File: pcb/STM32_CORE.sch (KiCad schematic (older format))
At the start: 31 parts, among them J6 Conn_01x14, J7 Conn_01x12, J8 Conn_01x12, SW1 SW_Push, U3 STM32F103C8T6, U4 AMS1117-3.3, Y1 O8M, Y2 O32.768K

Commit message: update,
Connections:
- net PA2 renamed IONAIR-TTL-TX
- net PA3 renamed IONAIR-TTL-RX
- net PA6 renamed STM32_WS2812_OUTPUT
- net PB0 renamed STM32_SSR-25-DA_OUTPUT
- net PB1 renamed STM32_SSR_OUTPUT
- net PB3 renamed SPI1_SCK
- net PB4 renamed SPI1_MISO
- net PB5 renamed SPI1_MOSI
- net PB6 renamed STM32_FAN_PWM_OUTPUT
- net PB8 renamed I2C_SCL
- net PB9 renamed I2C_SDA
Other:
- moved on the sheet: C2, C3, C4, C5, C6
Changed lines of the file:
@@
 L taobao-c:C104 C3
 U 1 1 5BCBC4D6
-P 7850 5850
-F 0 "C3" H 7942 5896 50  0000 L CNN
-F 1 "C104" H 7942 5805 50  0000 L CNN
-F 2 "Capacitor_SMD:C_0603_1608Metric_Pad1.05x0.95mm_HandSolder" H 7850 5850 50  0001 C CNN
-F 3 "~" H 7850 5850 50  0001 C CNN
-	1    7850 5850
-	1    0    0    -1
-$EndComp
-Wire Wire Line
-	7850 5650 7850 5750
+P 7850 6800
+F 0 "C3" H 7942 6846 50  0000 L CNN
+F 1 "C104" H 7942 6755 50  0000 L CNN
+F 2 "Capacitor_SMD:C_0603_1608Metric_Pad1.05x0.95mm_HandSolder" H 7850 6800 50  0001 C CNN
+F 3 "~" H 7850 6800 50  0001 C CNN
+	1    7850 6800
+	1    0    0    -1
+$EndComp
+Wire Wire Line
+	7850 6600 7850 6700
 $Comp
 L power:GND #PWR026
 U 1 1 5BCBCE91
-P 7850 6050
-F 0 "#PWR026" H 7850 5800 50  0001 C CNN
-F 1 "GND" H 7855 5877 50  0000 C CNN
-F 2 "" H 7850 6050 50  0001 C CNN
-F 3 "" H 7850 6050 50  0001 C CNN
-	1    7850 6050
-	1    0    0    -1
-$EndComp
-Wire Wire Line
-	7850 5950 7850 6050
+P 7850 7000
+F 0 "#PWR026" H 7850 6750 50  0001 C CNN
+F 1 "GND" H 7855 6827 50  0000 C CNN
+F 2 "" H 7850 7000 50  0001 C CNN
+F 3 "" H 7850 7000 50  0001 C CNN
+	1    7850 7000
+	1    0    0    -1
+$EndComp
+Wire Wire Line
+	7850 6900 7850 7000
 $Comp
 L taobao-c:C104 C4
 U 1 1 5BCBD860
-P 8300 5850
-F 0 "C4" H 8392 5896 50  0000 L CNN
-F 1 "C104" H 8392 5805 50  0000 L CNN
-F 2 "Capacitor_SMD:C_0603_1608Metric_Pad1.05x0.95mm_HandSolder" H 8300 5850 50  0001 C CNN
-F 3 "~" H 8300 5850 50  0001 C CNN
-	1    8300 5850
-	1    0    0    -1
-$EndComp
-Wire Wire Line
-	8300 5650 8300 5750
+P 8300 6800
+F 0 "C4" H 8392 6846 50  0000 L CNN
+F 1 "C104" H 8392 6755 50  0000 L CNN
+F 2 "Capacitor_SMD:C_0603_1608Metric_Pad1.05x0.95mm_HandSolder" H 8300 6800 50  0001 C CNN
+F 3 "~" H 8300 6800 50  0001 C CNN
+	1    8300 6800
+	1    0    0    -1
+$EndComp
+Wire Wire Line
+	8300 6600 8300 6700
 $Comp
 L power:GND #PWR028
 U 1 1 5BCBD867
-P 8300 6050
-F 0 "#PWR028" H 8300 5800 50  0001 C CNN
-F 1 "GND" H 8305 5877 50  0000 C CNN
-F 2 "" H 8300 6050 50  0001 C CNN
-F 3 "" H 8300 6050 50  0001 C CNN
-	1    8300 6050
-	1    0    0    -1
-$EndComp
-Wire Wire Line
-	8300 5950 8300 6050
+P 8300 7000
+F 0 "#PWR028" H 8300 6750 50  0001 C CNN
+F 1 "GND" H 8305 6827 50  0000 C CNN
+F 2 "" H 8300 7000 50  0001 C CNN
+F 3 "" H 8300 7000 50  0001 C CNN
+	1    8300 7000
+	1    0    0    -1
+$EndComp
+Wire Wire Line
+	8300 6900 8300 7000
 $Comp
 L taobao-c:C104 C5
 U 1 1 5BCBE2F2
-P 8700 5850
-F 0 "C5" H 8792 5896 50  0000 L CNN
-F 1 "C104" H 8792 5805 50  0000 L CNN
-F 2 "Capacitor_SMD:C_0603_1608Metric_Pad1.05x0.95mm_HandSolder" H 8700 5850 50  0001 C CNN
-F 3 "~" H 8700 5850 50  0001 C CNN
-	1    8700 5850
-	1    0    0    -1
-$EndComp
-Wire Wire Line
-	8700 5650 8700 5750
+P 8700 6800
+F 0 "C5" H 8792 6846 50  0000 L CNN
+F 1 "C104" H 8792 6755 50  0000 L CNN
+F 2 "Capacitor_SMD:C_0603_1608Metric_Pad1.05x0.95mm_HandSolder" H 8700 6800 50  0001 C CNN
+F 3 "~" H 8700 6800 50  0001 C CNN
+	1    8700 6800
+	1    0    0    -1
+$EndComp
+Wire Wire Line
+	8700 6600 8700 6700
 $Comp
 L power:GND #PWR030
 U 1 1 5BCBE2F9
-P 8700 6050
-F 0 "#PWR030" H 8700 5800 50  0001 C CNN
-F 1 "GND" H 8705 5877 50  0000 C CNN
-F 2 "" H 8700 6050 50  0001 C CNN
-F 3 "" H 8700 6050 50  0001 C CNN
-	1    8700 6050
-	1    0    0    -1
-$EndComp
-Wire Wire Line
-	8700 5950 8700 6050
+P 8700 7000
+F 0 "#PWR030" H 8700 6750 50  0001 C CNN
+F 1 "GND" H 8705 6827 50  0000 C CNN
+F 2 "" H 8700 7000 50  0001 C CNN
+F 3 "" H 8700 7000 50  0001 C CNN
+	1    8700 7000
+	1    0    0    -1
+$EndComp
+Wire Wire Line
+	8700 6900 8700 7000
 $Comp
 L taobao-c:C104 C6
 U 1 1 5BCBE306
-P 9150 5850
-F 0 "C6" H 9242 5896 50  0000 L CNN
-F 1 "C104" H 9242 5805 50  0000 L CNN
-F 2 "Capacitor_SMD:C_0603_1608Metric_Pad1.05x0.95mm_HandSolder" H 9150 5850 50  0001 C CNN
-F 3 "~" H 9150 5850 50  0001 C CNN
-	1    9150 5850
-	1    0    0    -1
-$EndComp
-Wire Wire Line
-	9150 5650 9150 5750
+P 9150 6800
+F 0 "C6" H 9242 6846 50  0000 L CNN
+F 1 "C104" H 9242 6755 50  0000 L CNN
+F 2 "Capacitor_SMD:C_0603_1608Metric_Pad1.05x0.95mm_HandSolder" H 9150 6800 50  0001 C CNN
+F 3 "~" H 9150 6800 50  0001 C CNN
+	1    9150 6800
+	1    0    0    -1
+$EndComp
+Wire Wire Line
+	9150 6600 9150 6700
 $Comp
 L power:GND #PWR032
 U 1 1 5BCBE30D
-P 9150 6050
-F 0 "#PWR032" H 9150 5800 50  0001 C CNN
-F 1 "GND" H 9155 5877 50  0000 C CNN
-F 2 "" H 9150 6050 50  0001 C CNN
-F 3 "" H 9150 6050 50  0001 C CNN
-	1    9150 6050
-	1    0    0    -1
-$EndComp
-Wire Wire Line
-	9150 5950 9150 6050
+P 9150 7000
+F 0 "#PWR032" H 9150 6750 50  0001 C CNN
+F 1 "GND" H 9155 6827 50  0000 C CNN
+F 2 "" H 9150 7000 50  0001 C CNN
+F 3 "" H 9150 7000 50  0001 C CNN
+	1    9150 7000
+	1    0    0    -1
+$EndComp
+Wire Wire Line
+	9150 6900 9150 7000
 $Comp
 L taobao-osc:O32.768K Y2
@@
 L taobao-c:C104 C2
 U 1 1 5BD956B7
-P 5950 2200
-F 0 "C2" H 6042 2246 50  0000 L CNN
-F 1 "C104" H 6042 2155 50  0000 L CNN
-F 2 "Capacitor_SMD:C_0603_1608Metric_Pad1.05x0.95mm_HandSolder" H 5950 2200 50  0001 C CNN
-F 3 "~" H 5950 2200 50  0001 C CNN
-F 4 "near SWD" H 5950 2200 50  0001 C CNN "Field4"
-	1    5950 2200
+P 5250 1550
+F 0 "C2" H 5342 1596 50  0000 L CNN
+F 1 "C104" H 5342 1505 50  0000 L CNN
+F 2 "Capacitor_SMD:C_0603_1608Metric_Pad1.05x0.95mm_HandSolder" H 5250 1550 50  0001 C CNN
+F 3 "~" H 5250 1550 50  0001 C CNN
+F 4 "near SWD" H 5250 1550 50  0001 C CNN "Field4"
+	1    5250 1550
 	1    0    0    -1
 $EndComp
@@
 L power:GND #PWR023
 U 1 1 5BD957D4
-P 5950 2450
-F 0 "#PWR023" H 5950 2200 50  0001 C CNN
-F 1 "GND" H 5955 2277 50  0000 C CNN
-F 2 "" H 5950 2450 50  0001 C CNN
-F 3 "" H 5950 2450 50  0001 C CNN
-	1    5950 2450
-	1    0    0    -1
-$EndComp
-Wire Wire Line
-	5950 2300 5950 2450
-Wire Wire Line
-	5950 1950 5950 2100
+P 5250 1800
+F 0 "#PWR023" H 5250 1550 50  0001 C CNN
+F 1 "GND" H 5255 1627 50  0000 C CNN
+F 2 "" H 5250 1800 50  0001 C CNN
+F 3 "" H 5250 1800 50  0001 C CNN
+	1    5250 1800
+	1    0    0    -1
+$EndComp
+Wire Wire Line
+	5250 1650 5250 1800
+Wire Wire Line
+	5250 1300 5250 1450
 Text Label 2350 2600 2    50   ~ 0
 SWIO
@@
 	1    0    0    1
 $EndComp
-Text Label 6300 2350 1    50   ~ 0
+Text Label 5600 1700 1    50   ~ 0
 VCC3V3
 Wire Wire Line
-	6300 1950 6300 2350
+	5600 1300 5600 1700
 $Comp
 L Device:Jumper_NO_Small JP1
@@
 L power:+3V3 #PWR024
 U 1 1 5BCAD5BF
-P 6300 1950
-F 0 "#PWR024" H 6300 1800 50  0001 C CNN
-F 1 "+3V3" H 6350 2150 50  0000 C CNN
-F 2 "" H 6300 1950 50  0001 C CNN
-F 3 "" H 6300 1950 50  0001 C CNN
-	1    6300 1950
+P 5600 1300
+F 0 "#PWR024" H 5600 1150 50  0001 C CNN
+F 1 "+3V3" H 5650 1500 50  0000 C CNN
+F 2 "" H 5600 1300 50  0001 C CNN
+F 3 "" H 5600 1300 50  0001 C CNN
+	1    5600 1300
 	1    0    0    -1
 $EndComp
@@
 L power:+3V3 #PWR025
 U 1 1 5BCBE3DE
-P 7850 5650
-F 0 "#PWR025" H 7850 5500 50  0001 C CNN
-F 1 "+3V3" H 7900 5850 50  0000 C CNN
-F 2 "" H 7850 5650 50  0001 C CNN
-F 3 "" H 7850 5650 50  0001 C CNN
-	1    7850 5650
+P 7850 6600
+F 0 "#PWR025" H 7850 6450 50  0001 C CNN
+F 1 "+3V3" H 7900 6800 50  0000 C CNN
+F 2 "" H 7850 6600 50  0001 C CNN
+F 3 "" H 7850 6600 50  0001 C CNN
+	1    7850 6600
 	1    0    0    -1
 $EndComp
@@
 L power:+3V3 #PWR027
 U 1 1 5BCE7C1D
-P 8300 5650
-F 0 "#PWR027" H 8300 5500 50  0001 C CNN
-F 1 "+3V3" H 8350 5850 50  0000 C CNN
-F 2 "" H 8300 5650 50  0001 C CNN
-F 3 "" H 8300 5650 50  0001 C CNN
-	1    8300 5650
+P 8300 6600
+F 0 "#PWR027" H 8300 6450 50  0001 C CNN
+F 1 "+3V3" H 8350 6800 50  0000 C CNN
+F 2 "" H 8300 6600 50  0001 C CNN
+F 3 "" H 8300 6600 50  0001 C CNN
+	1    8300 6600
 	1    0    0    -1
 $EndComp
@@
 L power:+3V3 #PWR029
 U 1 1 5BCE7C66
-P 8700 5650
-F 0 "#PWR029" H 8700 5500 50  0001 C CNN
-F 1 "+3V3" H 8750 5850 50  0000 C CNN
-F 2 "" H 8700 5650 50  0001 C CNN
-F 3 "" H 8700 5650 50  0001 C CNN
-	1    8700 5650
+P 8700 6600
+F 0 "#PWR029" H 8700 6450 50  0001 C CNN
+F 1 "+3V3" H 8750 6800 50  0000 C CNN
+F 2 "" H 8700 6600 50  0001 C CNN
+F 3 "" H 8700 6600 50  0001 C CNN
+	1    8700 6600
 	1    0    0    -1
 $EndComp
@@
 L power:+3V3 #PWR031
 U 1 1 5BCE7CAF
-P 9150 5650
-F 0 "#PWR031" H 9150 5500 50  0001 C CNN
-F 1 "+3V3" H 9200 5850 50  0000 C CNN
-F 2 "" H 9150 5650 50  0001 C CNN
-F 3 "" H 9150 5650 50  0001 C CNN
-	1    9150 5650
+P 9150 6600
+F 0 "#PWR031" H 9150 6450 50  0001 C CNN
+F 1 "+3V3" H 9200 6800 50  0000 C CNN
+F 2 "" H 9150 6600 50  0001 C CNN
+F 3 "" H 9150 6600 50  0001 C CNN
+	1    9150 6600
 	1    0    0    -1
 $EndComp
@@
 L power:+3V3 #PWR022
 U 1 1 5BCF284B
-P 5950 1950
-F 0 "#PWR022" H 5950 1800 50  0001 C CNN
-F 1 "+3V3" H 6000 2150 50  0000 C CNN
-F 2 "" H 5950 1950 50  0001 C CNN
-F 3 "" H 5950 1950 50  0001 C CNN
-	1    5950 1950
+P 5250 1300
+F 0 "#PWR022" H 5250 1150 50  0001 C CNN
+F 1 "+3V3" H 5300 1500 50  0000 C CNN
+F 2 "" H 5250 1300 50  0001 C CNN
+F 3 "" H 5250 1300 50  0001 C CNN
+	1    5250 1300
 	1    0    0    -1
 $EndComp
@@
 	0    -1   -1   0
 $EndComp
+Text GLabel 8100 1650 1    50   Input ~ 0
+I2C_SDA
+Text GLabel 8200 1650 1    50   Input ~ 0
+I2C_SCL
+Text GLabel 8600 1650 1    50   Input ~ 0
+SPI1_MOSI
+Text GLabel 8700 1650 1    50   Input ~ 0
+SPI1_MISO
+Text GLabel 8800 1650 1    50   Input ~ 0
+SPI1_SCK
+Text GLabel 8500 1650 1    50   Input ~ 0
+STM32_FAN_PWM_OUTPUT
+Text GLabel 8500 4750 3    50   Input ~ 0
+STM32_SSR_OUTPUT
+Text GLabel 8400 4750 3    50   Input ~ 0
+STM32_SSR-25-DA_OUTPUT
+Text GLabel 6900 3750 0    50   Input ~ 0
+IONAIR-TTL-TX
+Text GLabel 7900 4750 3    50   Input ~ 0
+IONAIR-TTL-RX
+Text GLabel 8200 4750 3    50   Input ~ 0
+STM32_WS2812_OUTPUT
 $EndSCHEMATC

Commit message: update,
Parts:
- J8: value Conn_01x12 -> Conn_01x15; footprint Connector_PinHeader_1.27mm:PinHeader_1x20_P1.27mm_Vertical -> Connector_PinHeader_1.27mm:PinHeader_1x15_P1.27mm_Vertical; symbol Connector_Generic:Conn_01x20 -> Connector_Generic:Conn_01x15
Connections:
- net PB13 is gone; now on net STM32_FAN_PWM_OUTPUT: J7.2 (Pin_2), U3.26 (PB13)
- net +3V3: now also J8.2 (Pin_2); no longer J8.3 (Pin_3)
- net GND: now also J8.1 (Pin_1); no longer J8.2 (Pin_2)
- net IONAIR-TTL-RX: now also J8.7 (Pin_7); no longer J8.12 (Pin_12)
- net IONAIR-TTL-TX: now also J8.6 (Pin_6); no longer J8.11 (Pin_11)
- net PA0: now also J8.4 (Pin_4); no longer J8.9 (Pin_9)
- net PA1: now also J8.5 (Pin_5); no longer J8.10 (Pin_10)
- net PA4: now also J8.8 (Pin_8); no longer J8.13 (Pin_13)
- net PA5: now also J8.9 (Pin_9); no longer J8.14 (Pin_14)
- net PA7: now also J8.11 (Pin_11); no longer J8.16 (Pin_16)
- net PB10: now also J8.14 (Pin_14); no longer J8.19 (Pin_19)
- net PB11: now also J8.15 (Pin_15); no longer J8.20 (Pin_20)
- net STM32_FAN_PWM_OUTPUT: no longer J6.9 (Pin_9), U3.42 (PB6)
- net STM32_SSR-25-DA_OUTPUT: now also J8.13 (Pin_13), U3.19 (PB1); no longer J8.17 (Pin_17), U3.18 (PB0)
- net STM32_SSR_OUTPUT: now also J8.12 (Pin_12), U3.18 (PB0); no longer J8.18 (Pin_18), U3.19 (PB1)
- net STM32_WS2812_OUTPUT: now also J8.10 (Pin_10); no longer J8.15 (Pin_15)
- new net PB6: J6.9 (Pin_9), U3.42 (PB6)
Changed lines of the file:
@@
 L power:GND #PWR019
 U 1 1 5BD5A437
-P 3850 4750
-F 0 "#PWR019" H 3850 4500 50  0001 C CNN
-F 1 "GND" H 3855 4577 50  0000 C CNN
-F 2 "" H 3850 4750 50  0001 C CNN
-F 3 "" H 3850 4750 50  0001 C CNN
-	1    3850 4750
+P 3850 4350
+F 0 "#PWR019" H 3850 4100 50  0001 C CNN
+F 1 "GND" H 3855 4177 50  0000 C CNN
+F 2 "" H 3850 4350 50  0001 C CNN
+F 3 "" H 3850 4350 50  0001 C CNN
+	1    3850 4350
 	1    0    0    -1
 $EndComp
@@
 $EndComp
 $Comp
-L Connector_Generic:Conn_01x20 J8
+L Connector_Generic:Conn_01x15 J8
 U 1 1 5BDCE49F
-P 4950 3900
-F 0 "J8" H 4869 2675 50  0000 C CNN
-F 1 "Conn_01x12" H 4869 2766 50  0000 C CNN
-F 2 "Connector_PinHeader_1.27mm:PinHeader_1x20_P1.27mm_Vertical" H 4950 3900 50  0001 C CNN
-F 3 "~" H 4950 3900 50  0001 C CNN
-	1    4950 3900
+P 4950 3600
+F 0 "J8" H 4869 2375 50  0000 C CNN
+F 1 "Conn_01x15" H 4869 2466 50  0000 C CNN
+F 2 "Connector_PinHeader_1.27mm:PinHeader_1x15_P1.27mm_Vertical" H 4950 3600 50  0001 C CNN
+F 3 "~" H 4950 3600 50  0001 C CNN
+	1    4950 3600
 	1    0    0    1
 $EndComp
@@
 	4350 3800 4750 3800
 Wire Wire Line
-	3850 4750 3850 4700
-Wire Wire Line
-	3850 4700 4750 4700
-Wire Wire Line
-	3950 4550 3950 4600
-Wire Wire Line
-	3950 4600 4750 4600
+	3850 4350 3850 4300
+Wire Wire Line
+	3850 4300 4750 4300
+Wire Wire Line
+	3950 4150 3950 4200
+Wire Wire Line
+	3950 4200 4750 4200
 Text Label 2000 3700 2    50   ~ 0
 PC13
@@
 L power:+3V3 #PWR020
 U 1 1 5BCACA2F
-P 3950 4550
-F 0 "#PWR020" H 3950 4400 50  0001 C CNN
-F 1 "+3V3" H 4000 4750 50  0000 C CNN
-F 2 "" H 3950 4550 50  0001 C CNN
-F 3 "" H 3950 4550 50  0001 C CNN
-	1    3950 4550
+P 3950 4150
+F 0 "#PWR020" H 3950 4000 50  0001 C CNN
+F 1 "+3V3" H 4000 4350 50  0000 C CNN
+F 2 "" H 3950 4150 50  0001 C CNN
+F 3 "" H 3950 4150 50  0001 C CNN
+	1    3950 4150
 	1    0    0    -1
 $EndComp
@@
 Text GLabel 8800 1650 1    50   Input ~ 0
 SPI1_SCK
-Text GLabel 8500 1650 1    50   Input ~ 0
+Text GLabel 10000 3650 2    50   Input ~ 0
 STM32_FAN_PWM_OUTPUT
+Text GLabel 8400 4750 3    50   Input ~ 0
+STM32_SSR_OUTPUT
 Text GLabel 8500 4750 3    50   Input ~ 0
-STM32_SSR_OUTPUT
-Text GLabel 8400 4750 3    50   Input ~ 0
 STM32_SSR-25-DA_OUTPUT
 Text GLabel 6900 3750 0    50   Input ~ 0

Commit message: update,
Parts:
- added J11: Conn_01x04, footprint-lib:Pin_Header_Straight_1x04_Pitch2.54mm, symbol Connector_Generic:Conn_01x04
- added J12: Conn_01x04, footprint-lib:Pin_Header_Straight_1x03_Pitch2.54mm, symbol Connector_Generic:Conn_01x03
- J6: footprint Connector_PinHeader_1.27mm:PinHeader_1x14_P1.27mm_Vertical -> footprint-lib:Pin_Header_Straight_1x14_Pitch1.27mm
- J7: footprint Connector_PinHeader_1.27mm:PinHeader_1x12_P1.27mm_Vertical -> footprint-lib:Pin_Header_Straight_1x12_Pitch1.27mm
- J8: footprint Connector_PinHeader_1.27mm:PinHeader_1x15_P1.27mm_Vertical -> footprint-lib:Pin_Header_Straight_1x15_Pitch1.27mm
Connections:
- net +3V3: now also J11.4 (Pin_4), J12.2 (Pin_2); no longer D2.2 (A), J6.1 (Pin_1)
- net +5V: now also D2.2 (A), J12.3 (Pin_3)
- net GND: now also J11.1 (Pin_1), J12.1 (Pin_1)
- net SWCLK: now also J11.2 (Pin_2)
- net SWIO: now also J11.3 (Pin_3)
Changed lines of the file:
@@
 Wire Wire Line
 	2250 3800 2250 3950
-Wire Wire Line
-	2150 2400 2150 2500
 $Comp
 L power:GND #PWR018
@@
 F 0 "J7" V 3467 1596 50  0000 C CNN
 F 1 "Conn_01x12" V 3376 1596 50  0000 C CNN
-F 2 "Connector_PinHeader_1.27mm:PinHeader_1x12_P1.27mm_Vertical" H 3250 1650 50  0001 C CNN
+F 2 "footprint-lib:Pin_Header_Straight_1x12_Pitch1.27mm" H 3250 1650 50  0001 C CNN
 F 3 "~" H 3250 1650 50  0001 C CNN
 	1    3250 1650
@@
 F 0 "J6" H 1420 3817 50  0000 C CNN
 F 1 "Conn_01x14" H 1420 3726 50  0000 C CNN
-F 2 "Connector_PinHeader_1.27mm:PinHeader_1x14_P1.27mm_Vertical" H 1500 3100 50  0001 C CNN
+F 2 "footprint-lib:Pin_Header_Straight_1x14_Pitch1.27mm" H 1500 3100 50  0001 C CNN
 F 3 "~" H 1500 3100 50  0001 C CNN
 	1    1500 3100
@@
 F 0 "J8" H 4869 2375 50  0000 C CNN
 F 1 "Conn_01x15" H 4869 2466 50  0000 C CNN
-F 2 "Connector_PinHeader_1.27mm:PinHeader_1x15_P1.27mm_Vertical" H 4950 3600 50  0001 C CNN
+F 2 "footprint-lib:Pin_Header_Straight_1x15_Pitch1.27mm" H 4950 3600 50  0001 C CNN
 F 3 "~" H 4950 3600 50  0001 C CNN
 	1    4950 3600
@@
 Wire Wire Line
 	1700 2600 2350 2600
-Wire Wire Line
-	1700 2500 2150 2500
 Text Label 4350 4000 0    50   ~ 0
 PA0
@@
 Wire Wire Line
 	2000 3700 1700 3700
-$Comp
-L power:+3V3 #PWR017
-U 1 1 5BCAC201
-P 2150 2400
-F 0 "#PWR017" H 2150 2250 50  0001 C CNN
-F 1 "+3V3" H 2200 2600 50  0000 C CNN
-F 2 "" H 2150 2400 50  0001 C CNN
-F 3 "" H 2150 2400 50  0001 C CNN
-	1    2150 2400
-	1    0    0    -1
-$EndComp
 $Comp
 L power:+3V3 #PWR020
@@
 F 3 "" H 13000 4800 50  0001 C CNN
 	1    13000 4800
-	1    0    0    -1
-$EndComp
-$Comp
-L power:+3V3 #PWR044
-U 1 1 5BCE8771
-P 14200 4750
-F 0 "#PWR044" H 14200 4600 50  0001 C CNN
-F 1 "+3V3" H 14250 4950 50  0000 C CNN
-F 2 "" H 14200 4750 50  0001 C CNN
-F 3 "" H 14200 4750 50  0001 C CNN
-	1    14200 4750
 	1    0    0    -1
 $EndComp
@@
 Text GLabel 8200 4750 3    50   Input ~ 0
 STM32_WS2812_OUTPUT
+$Comp
+L Connector_Generic:Conn_01x04 J11
+U 1 1 5BD063FA
+P 1500 1850
+F 0 "J11" H 1420 1425 50  0000 C CNN
+F 1 "Conn_01x04" H 1420 1516 50  0000 C CNN
+F 2 "footprint-lib:Pin_Header_Straight_1x04_Pitch2.54mm" H 1500 1850 50  0001 C CNN
+F 3 "~" H 1500 1850 50  0001 C CNN
+	1    1500 1850
+	-1   0    0    1
+$EndComp
+Wire Wire Line
+	2150 1550 2150 1650
+$Comp
+L power:GND #PWR0109
+U 1 1 5BD06547
+P 2150 2050
+F 0 "#PWR0109" H 2150 1800 50  0001 C CNN
+F 1 "GND" H 2155 1877 50  0000 C CNN
+F 2 "" H 2150 2050 50  0001 C CNN
+F 3 "" H 2150 2050 50  0001 C CNN
+	1    2150 2050
+	1    0    0    -1
+$EndComp
+Wire Wire Line
+	2150 1950 2150 2050
+Text Label 2350 1750 2    50   ~ 0
+SWIO
+Text Label 2350 1850 2    50   ~ 0
+SWCLK
+Wire Wire Line
+	1700 1950 2150 1950
+Wire Wire Line
+	1700 1850 2350 1850
+Wire Wire Line
+	1700 1750 2350 1750
+Wire Wire Line
+	1700 1650 2150 1650
+$Comp
+L power:+3V3 #PWR0110
+U 1 1 5BD06554
+P 2150 1550
+F 0 "#PWR0110" H 2150 1400 50  0001 C CNN
+F 1 "+3V3" H 2200 1750 50  0000 C CNN
+F 2 "" H 2150 1550 50  0001 C CNN
+F 3 "" H 2150 1550 50  0001 C CNN
+	1    2150 1550
+	1    0    0    -1
+$EndComp
+$Comp
+L Connector_Generic:Conn_01x03 J12
+U 1 1 5BD193F5
+P 1600 5650
+F 0 "J12" H 1520 5325 50  0000 C CNN
+F 1 "Conn_01x04" H 1520 5416 50  0000 C CNN
+F 2 "footprint-lib:Pin_Header_Straight_1x03_Pitch2.54mm" H 1600 5650 50  0001 C CNN
+F 3 "~" H 1600 5650 50  0001 C CNN
+	1    1600 5650
+	-1   0    0    1
+$EndComp
+$Comp
+L power:GND #PWR0111
+U 1 1 5BD194D7
+P 2250 5850
+F 0 "#PWR0111" H 2250 5600 50  0001 C CNN
+F 1 "GND" H 2255 5677 50  0000 C CNN
+F 2 "" H 2250 5850 50  0001 C CNN
+F 3 "" H 2250 5850 50  0001 C CNN
+	1    2250 5850
+	1    0    0    -1
+$EndComp
+Wire Wire Line
+	2250 5750 2250 5850
+Wire Wire Line
+	1800 5750 2250 5750
+Wire Wire Line
+	2650 5750 2250 5650
+Wire Wire Line
+	1800 5650 2250 5650
+$Comp
+L power:+3V3 #PWR0112
+U 1 1 5BD22354
+P 2650 5750
+F 0 "#PWR0112" H 2650 5600 50  0001 C CNN
+F 1 "+3V3" H 2700 5950 50  0000 C CNN
+F 2 "" H 2650 5750 50  0001 C CNN
+F 3 "" H 2650 5750 50  0001 C CNN
+	1    2650 5750
+	1    0    0    -1
+$EndComp
+$Comp
+L customized_power:+5V #PWR0113
+U 1 1 5BD34E07
+P 2350 5500
+F 0 "#PWR0113" H 2350 5350 50  0001 C CNN
+F 1 "+5V" H 2400 5700 50  0000 C CNN
+F 2 "" H 2350 5500 50  0001 C CNN
+F 3 "" H 2350 5500 50  0001 C CNN
+	1    2350 5500
+	1    0    0    -1
+$EndComp
+Wire Wire Line
+	2350 5500 2350 5550
+Wire Wire Line
+	2350 5550 1800 5550
+$Comp
+L tinkerforge:+5V #PWR0114
+U 1 1 5BD3EFE4
+P 14200 4750
+F 0 "#PWR0114" H 14200 4600 50  0001 C CNN
+F 1 "+5V" H 14215 4923 50  0000 C CNN
+F 2 "" H 14200 4750 50  0000 C CNN
+F 3 "" H 14200 4750 50  0000 C CNN
+	1    14200 4750
+	1    0    0    -1
+$EndComp
 $EndSCHEMATC

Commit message: add .gitignore .gitattributes,
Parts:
- removed Y2: O32.768K, Crystal:Crystal_SMD_MicroCrystal_CC7V-T1A-2Pin_3.2x1.5mm_HandSoldering, symbol taobao-osc:O32.768K
- added Y2: O_EPSON_32.768K, footprint-lib:MC-306, symbol taobao-osc:O_EPSON_32.768K
- SW1: footprint Button_Switch_SMD:SW_SPST_CK_RS282G05A3 -> Button_Switch_SMD:SW_SPST_PTS645
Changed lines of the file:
@@
 	9150 6900 9150 7000
-$Comp
-L taobao-osc:O32.768K Y2
-U 1 1 5BCBF11C
-P 14700 7500
-F 0 "Y2" V 14654 7588 50  0000 L CNN
-F 1 "O32.768K" V 14745 7588 50  0000 L CNN
-F 2 "Crystal:Crystal_SMD_MicroCrystal_CC7V-T1A-2Pin_3.2x1.5mm_HandSoldering" H 14700 7500 50  0001 C CNN
-F 3 "~" H 14700 7500 50  0001 C CNN
-	1    14700 7500
-	0    1    1    0
-$EndComp
 $Comp
 L taobao-c:C20pf C13
@@
 F 0 "SW1" V 14246 3248 50  0000 L CNN
 F 1 "SW_Push" V 14155 3248 50  0000 L CNN
-F 2 "Button_Switch_SMD:SW_SPST_CK_RS282G05A3" H 14200 3300 50  0001 C CNN
+F 2 "Button_Switch_SMD:SW_SPST_PTS645" H 14200 3300 50  0001 C CNN
 F 3 "" H 14200 3300 50  0001 C CNN
 	1    14200 3100
@@
 	1    0    0    -1
 $EndComp
+$Comp
+L taobao-osc:O_EPSON_32.768K Y2
+U 1 1 5BD58864
+P 14700 7500
+F 0 "Y2" V 14746 7588 50  0000 L CNN
+F 1 "O_EPSON_32.768K" V 14655 7588 50  0000 L CNN
+F 2 "footprint-lib:MC-306" H 14700 7500 50  0001 C CNN
+F 3 "https://support.epson.biz/td/api/doc_check.php?dl=brief_MC-306&lang=en" H 14700 7500 50  0001 C CNN
+	1    14700 7500
+	0    1    -1   0
+$EndComp
 $EndSCHEMATC

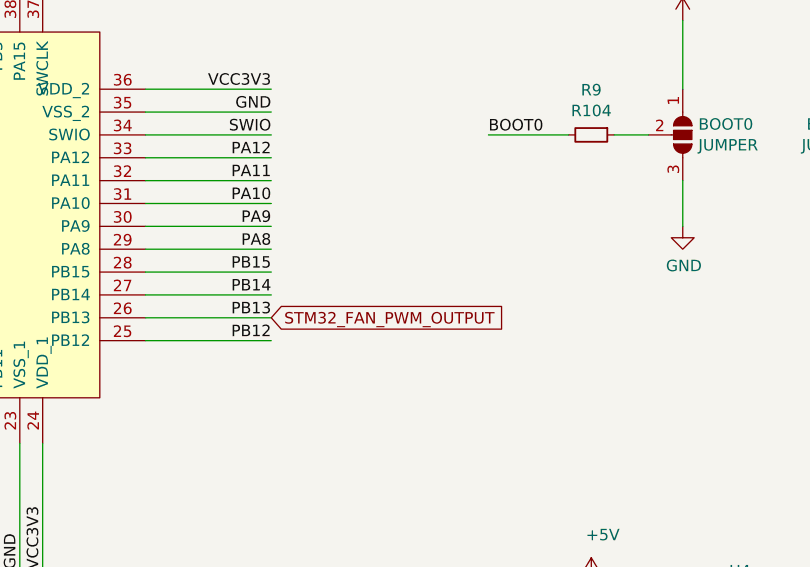
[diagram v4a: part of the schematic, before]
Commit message: update FAN PWM to PA8
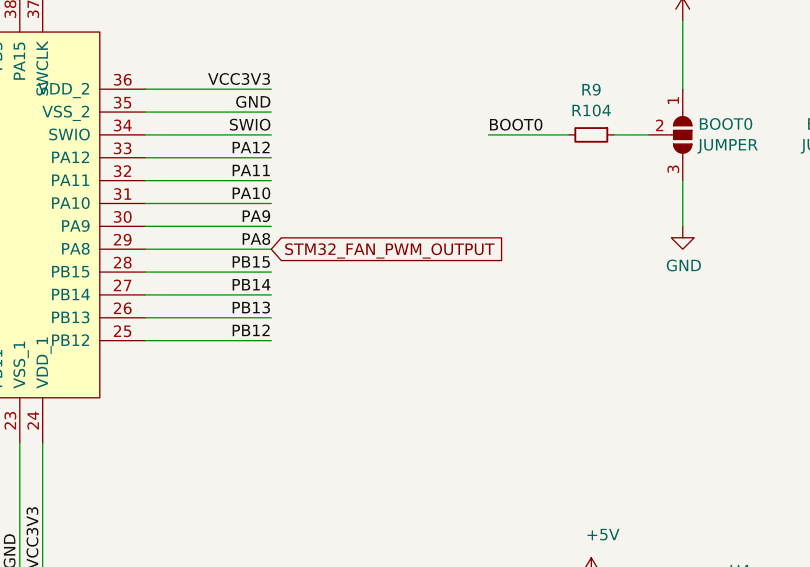
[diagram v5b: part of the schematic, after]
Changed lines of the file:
@@
 Text GLabel 8800 1650 1    50   Input ~ 0
 SPI1_SCK
-Text GLabel 10000 3650 2    50   Input ~ 0
+Text GLabel 10000 3350 2    50   Input ~ 0
 STM32_FAN_PWM_OUTPUT
 Text GLabel 8400 4750 3    50   Input ~ 0
